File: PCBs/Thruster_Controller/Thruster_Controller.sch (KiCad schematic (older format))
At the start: 30 parts, among them J1 PHASE_A, J2 PHASE_B, J3 PHASE_C, J4 Conn_01x01, J5 Pogo Conn, J6 Conn_01x01, J7 PWRIN, U2 RTQ2569-50GQW, U3 MCP2515, U8 MCP2562, Y1 20MHz

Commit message: Layout
- Trying out different layout approaches
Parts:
- removed J7: PWRIN, MCU_Powertrain:AMASS_XT60-M, symbol Connector_Generic:Conn_01x02
- added J? (x2): Conn_01x01, symbol Connector_Generic:Conn_01x01
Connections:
- net +BATT: now also J?.1 (Pin_1)
- net GND: now also J?.1 (Pin_1)
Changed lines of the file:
@@
 Text Notes 2260 5050 0    79   Italic 16
 3.3V Regulator
-$Comp
-L Connector_Generic:Conn_01x02 J7
-U 1 1 5E5819AC
-P 965 5235
-F 0 "J7" H 965 5010 50  0000 C CNN
-F 1 "PWRIN" H 890 5385 50  0001 C CNN
-F 2 "MCU_Powertrain:AMASS_XT60-M" H 965 5235 50  0001 C CNN
-F 3 "~" H 965 5235 50  0001 C CNN
-F 4 "" H 965 5235 50  0001 C CNN "Digikey"
-	1    965  5235
-	-1   0    0    1
-$EndComp
 Wire Wire Line
 	1365 5085 1365 5135
@@
 $EndComp
 Wire Wire Line
-	1165 5235 1365 5235
-Wire Wire Line
-	1365 5235 1365 5285
+	1165 5260 1365 5260
+Wire Wire Line
+	1365 5260 1365 5310
 $Comp
 L power:GND #PWR?
 U 1 1 5E585248
-P 1365 5285
+P 1365 5310
 AR Path="/5E20A2BB/5E585248" Ref="#PWR?"  Part="1"
 AR Path="/5E585248" Ref="#PWR0111"  Part="1"
-F 0 "#PWR0111" H 1365 5035 50  0001 C CNN
-F 1 "GND" H 1515 5210 50  0000 C CNN
-F 2 "" H 1365 5285 50  0001 C CNN
-F 3 "" H 1365 5285 50  0001 C CNN
-	1    1365 5285
+F 0 "#PWR0111" H 1365 5060 50  0001 C CNN
+F 1 "GND" H 1515 5235 50  0000 C CNN
+F 2 "" H 1365 5310 50  0001 C CNN
+F 3 "" H 1365 5310 50  0001 C CNN
+	1    1365 5310
 	1    0    0    -1
 $EndComp
@@
 	1    0    0    -1
 $EndComp
+$Comp
+L Connector_Generic:Conn_01x01 J?
+U 1 1 5EED2A54
+P 965 5135
+F 0 "J?" H 1130 5140 50  0000 C CNN
+F 1 "Conn_01x01" H 883 5001 50  0001 C CNN
+F 2 "" H 965 5135 50  0001 C CNN
+F 3 "~" H 965 5135 50  0001 C CNN
+	1    965  5135
+	-1   0    0    1
+$EndComp
+$Comp
+L Connector_Generic:Conn_01x01 J?
+U 1 1 5EED568B
+P 965 5260
+F 0 "J?" H 1135 5265 50  0000 C CNN
+F 1 "Conn_01x01" H 883 5126 50  0001 C CNN
+F 2 "" H 965 5260 50  0001 C CNN
+F 3 "~" H 965 5260 50  0001 C CNN
+	1    965  5260
+	-1   0    0    1
+$EndComp
 $EndSCHEMATC

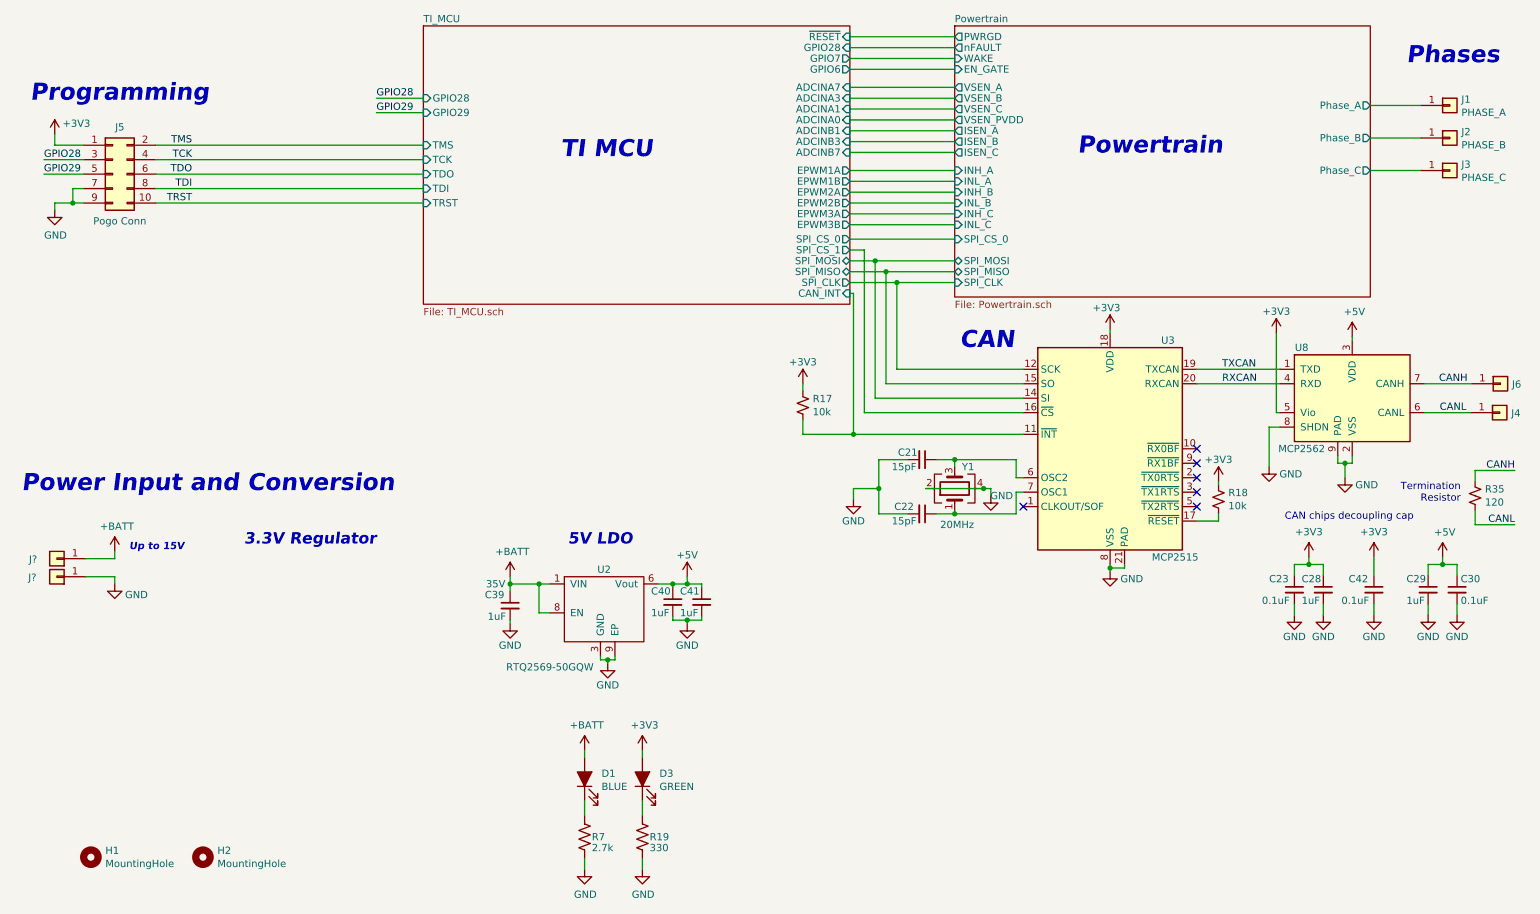
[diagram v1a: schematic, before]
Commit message: 3V3 Regulator
- Added in new 3V3 switching regulator, should save $$$ from the old one and about 1W versus a standard LDO
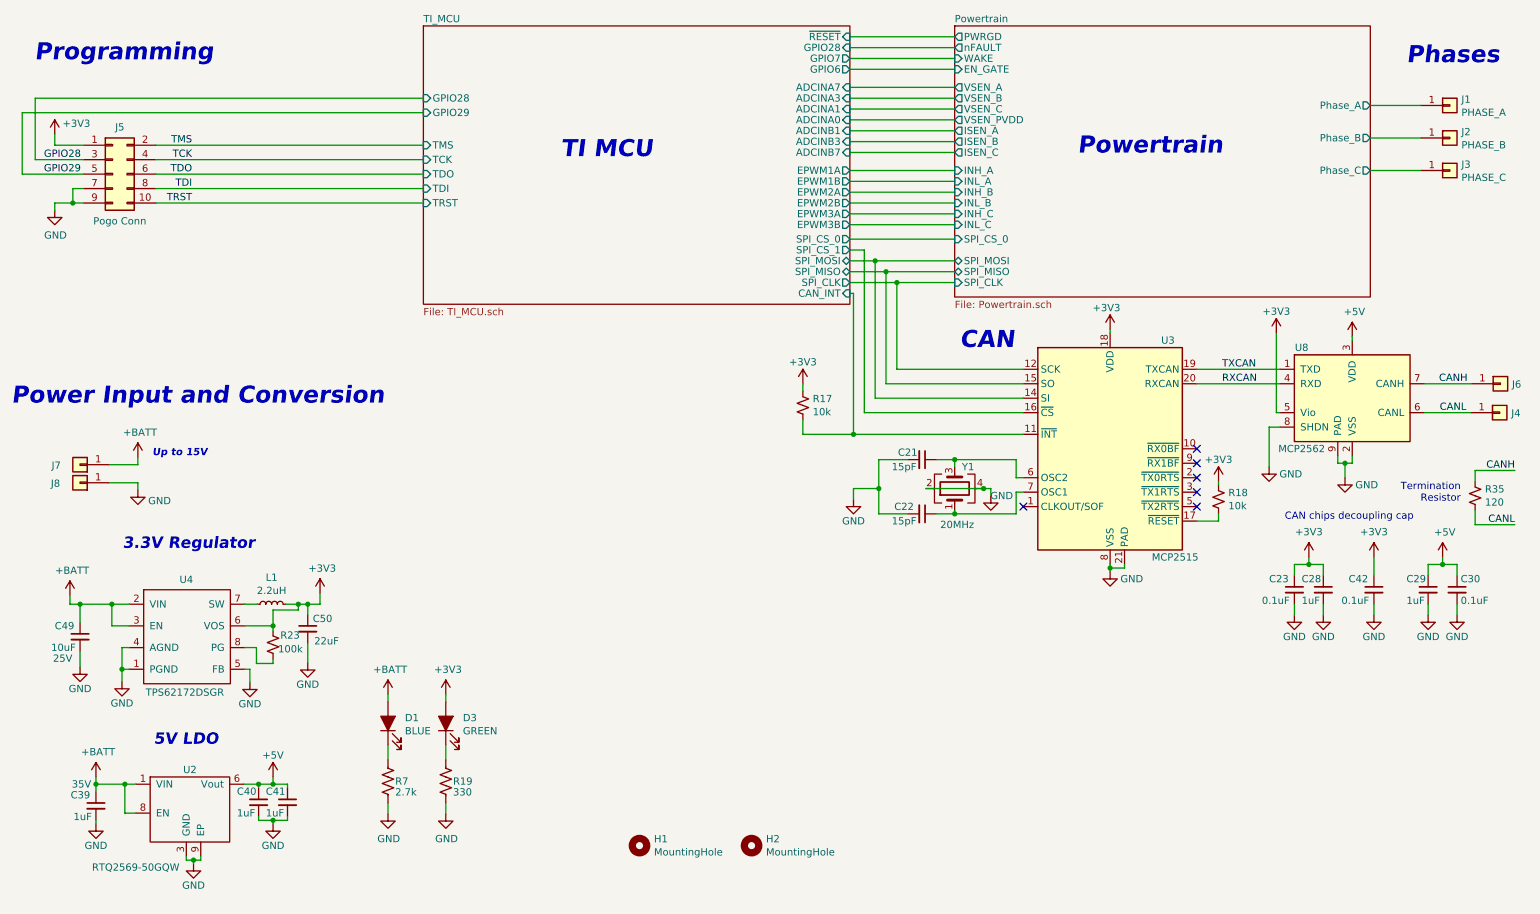
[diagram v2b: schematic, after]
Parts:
- added C49: 10uF, Capacitors_SMD:C_0805, symbol Device:C_Small
- added C50: 22uF, Capacitors_SMD:C_0603, symbol Device:C_Small
- added L1: 2.2uH, Inductors_SMD:L_0805, symbol Device:L_Small
- added R23: 100k, Resistors_SMD:R_0402_NoSilk, symbol Device:R_Small_US
- added U4: TPS62172DSGR, Thruster_Controller:8-Pin_WSON, symbol Thruster_Controller:TPS62172DSGR
- gave numbers to parts that had none: 2
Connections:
- net +3V3: now also C50.1, L1.2, R23.1, U4.6 (VOS)
- net +BATT: now also C49.1, U4.2 (VIN), U4.3 (EN)
- net GND: now also C49.2, C50.2, U4.1 (PGND), U4.4 (AGND), U4.5 (FB)
- new net: L1.1, U4.7 (SW)
- new net: R23.2, U4.8 (PG)
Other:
- moved on the sheet: C39, C40, C41, D1, D3, H1, H2, J7, J8, R19, R7, U2

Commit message: More Layout and Routing
- Powertrain is mostly done, very tight and the phase and bus pads are sized and placed!
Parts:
- J1, J2, J3: footprint MCU_Powertrain:3mm_Bullet_RA -> Thruster_Controller:Phase_Pad
- J7, J8: footprint (none) -> Thruster_Controller:Bus_Pad
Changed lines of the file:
@@
 F 0 "J1" H 10680 2042 50  0000 L CNN
 F 1 "PHASE_A" H 10680 1951 50  0000 L CNN
-F 2 "MCU_Powertrain:3mm_Bullet_RA" H 10600 2000 50  0001 C CNN
+F 2 "Thruster_Controller:Phase_Pad" H 10600 2000 50  0001 C CNN
 F 3 "~" H 10600 2000 50  0001 C CNN
 	1    10600 2000
@@
 F 0 "J2" H 10680 2267 50  0000 L CNN
 F 1 "PHASE_B" H 10680 2176 50  0000 L CNN
-F 2 "MCU_Powertrain:3mm_Bullet_RA" H 10600 2225 50  0001 C CNN
+F 2 "Thruster_Controller:Phase_Pad" H 10600 2225 50  0001 C CNN
 F 3 "~" H 10600 2225 50  0001 C CNN
 	1    10600 2225
@@
 F 0 "J3" H 10680 2492 50  0000 L CNN
 F 1 "PHASE_C" H 10680 2401 50  0000 L CNN
-F 2 "MCU_Powertrain:3mm_Bullet_RA" H 10600 2450 50  0001 C CNN
+F 2 "Thruster_Controller:Phase_Pad" H 10600 2450 50  0001 C CNN
 F 3 "~" H 10600 2450 50  0001 C CNN
 	1    10600 2450
@@
 F 0 "J7" H 1290 4490 50  0000 C CNN
 F 1 "Conn_01x01" H 1043 4351 50  0001 C CNN
-F 2 "" H 1125 4485 50  0001 C CNN
+F 2 "Thruster_Controller:Bus_Pad" H 1125 4485 50  0001 C CNN
 F 3 "~" H 1125 4485 50  0001 C CNN
 	1    1125 4485
@@
 F 0 "J8" H 1295 4615 50  0000 C CNN
 F 1 "Conn_01x01" H 1043 4476 50  0001 C CNN
-F 2 "" H 1125 4610 50  0001 C CNN
+F 2 "Thruster_Controller:Bus_Pad" H 1125 4610 50  0001 C CNN
 F 3 "~" H 1125 4610 50  0001 C CNN
 	1    1125 4610

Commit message: More Layout + Routing
- Added 3V3 converter
- Moved DRV passives to directly underneath DRV chip on top layer
- Fit power indication LEDs!
- Think there should be enough space for everything! Routing to the left of TI chip and CAN controller to the right
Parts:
- H1, H2: footprint Mounting_Holes:MountingHole_2.2mm_M2 -> Thruster_Controller:MountingHole_M2
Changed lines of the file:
@@
 F 0 "H2" H 5870 7166 50  0000 L CNN
 F 1 "MountingHole" H 5870 7075 50  0000 L CNN
-F 2 "Mounting_Holes:MountingHole_2.2mm_M2" H 5770 7120 50  0001 C CNN
+F 2 "Thruster_Controller:MountingHole_M2" H 5770 7120 50  0001 C CNN
 F 3 "~" H 5770 7120 50  0001 C CNN
 	1    5770 7120
@@
 F 0 "H1" H 5095 7166 50  0000 L CNN
 F 1 "MountingHole" H 5095 7075 50  0000 L CNN
-F 2 "Mounting_Holes:MountingHole_2.2mm_M2" H 4995 7120 50  0001 C CNN
+F 2 "Thruster_Controller:MountingHole_M2" H 4995 7120 50  0001 C CNN
 F 3 "~" H 4995 7120 50  0001 C CNN
 	1    4995 7120

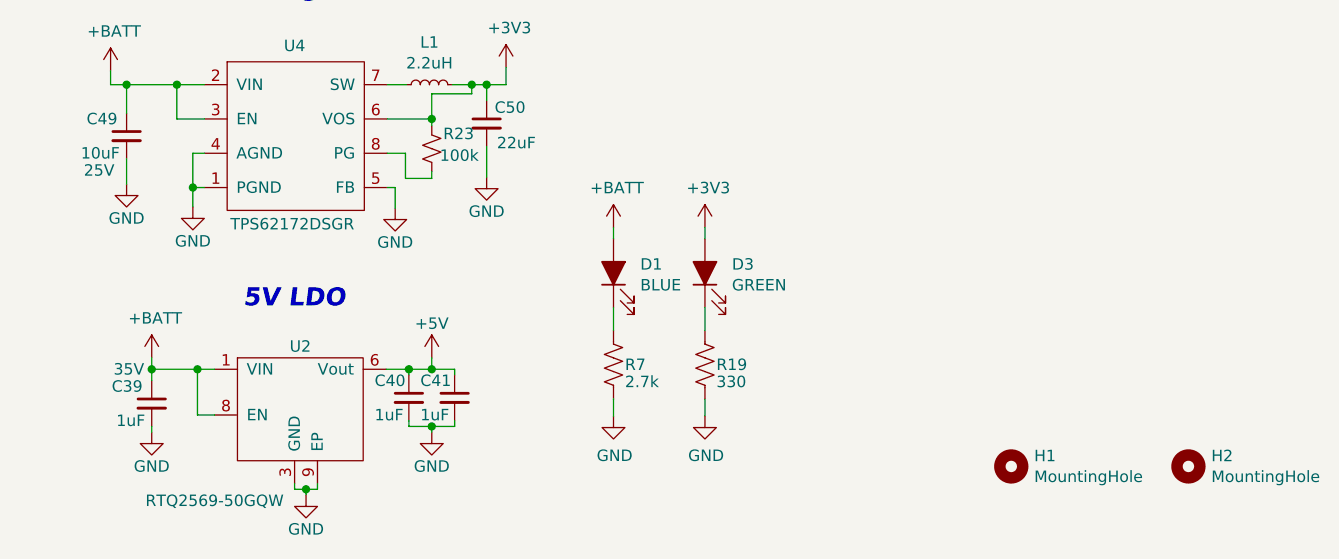
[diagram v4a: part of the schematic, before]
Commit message: Initial Routing Finished
- All layout and routing initially finished
- Still need to clean up silkscreen and any routing blemishes
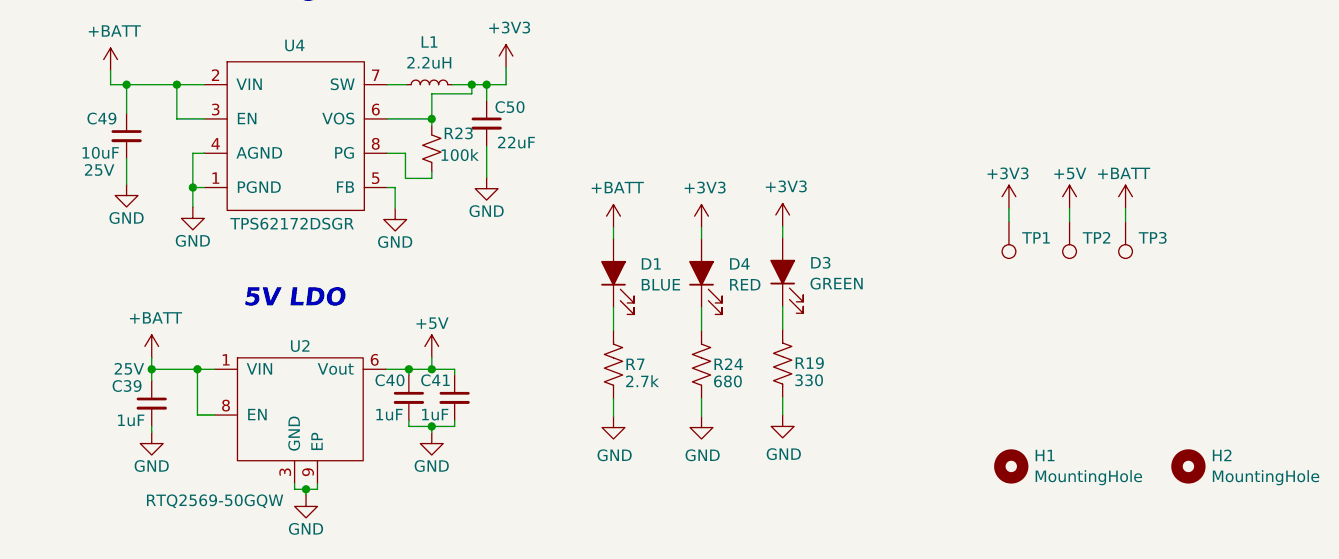
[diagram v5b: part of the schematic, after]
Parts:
- added D4: RED, LEDs:LED_0603, symbol Device:LED_ALT
- added R24: 680, Resistors_SMD:R_0603, symbol Device:R_US
- added TP1, TP2, TP3: TestPoint, Thruster_Controller:TestPoint_Pad_D1.0mm, symbol Connector:TestPoint
- C21: footprint Capacitors_SMD:C_0603 -> Capacitors_SMD:C_0402
- C22: footprint Capacitors_SMD:C_0603 -> Capacitors_SMD:C_0402; Digikey 311-1060-1-ND -> 732-7456-1-ND
- C23, C30, C42: footprint Capacitors_SMD:C_0603 -> Capacitors_SMD:C_0402; Digikey 1276-CL10B104KB8NNNLCT-ND -> 490-10698-1-ND
- C28, C29, C40, C41: footprint Capacitors_SMD:C_0805 -> Capacitors_SMD:C_0603; Digikey 399-8011-1-ND -> 1276-1102-1-ND
- C39: footprint Capacitors_SMD:C_0805 -> Capacitors_SMD:C_0603; Digikey 311-1909-1-ND -> 1276-1102-1-ND; Voltage 35V -> 25V
- D1: Digikey 160-1827-1-ND -> 732-4966-1-ND
- D3: Digikey 160-1446-1-ND -> 732-4980-1-ND
- J4, J6: footprint (none) -> Thruster_Controller:CAN_Pad
- R17, R18: footprint Resistors_SMD:R_0805 -> Resistors_SMD:R_0402; Digikey 311-10.0KCRCT-ND -> 311-10KJRCT-ND
- R35: footprint Resistors_SMD:R_0805 -> Resistors_SMD:R_0402; Digikey A129738CT-ND -> 311-120JRCT-ND
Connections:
- net +3V3: now also D4.2 (A), TP1.1
- net +5V: now also TP2.1
- net +BATT: now also TP3.1
- net GND: now also R24.2
- new net: D4.1 (K), R24.1
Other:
- moved on the sheet: D3, R19

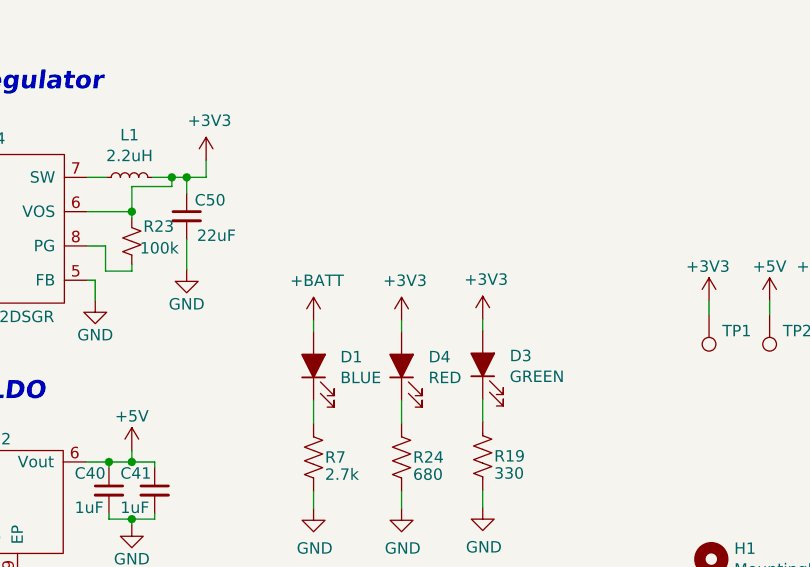
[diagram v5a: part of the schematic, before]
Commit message: Silk and Routing
- Fixed 5V LED indicator
- Small layout and routing cleanups
- Cleaned up Silkscreen
- Board is "finished" !!
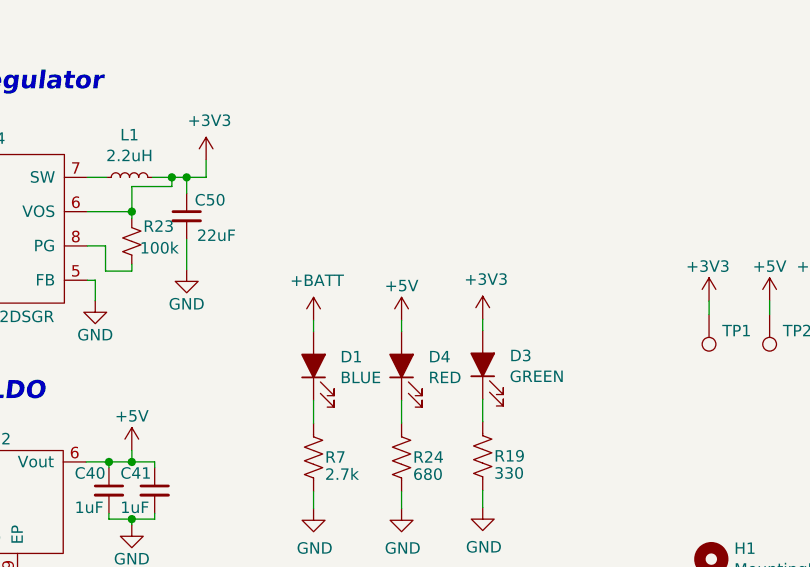
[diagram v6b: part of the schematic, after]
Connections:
- net +3V3: no longer D4.2 (A)
- net +5V: now also D4.2 (A)
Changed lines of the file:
@@
 	3995 6120 3995 6070
-$Comp
-L power:+3V3 #PWR?
-U 1 1 5E5672BA
-P 3995 6070
-AR Path="/5E20A2BB/5E5672BA" Ref="#PWR?"  Part="1"
-AR Path="/5E5672BA" Ref="#PWR0108"  Part="1"
-F 0 "#PWR0108" H 3995 5920 50  0001 C CNN
-F 1 "+3V3" H 4010 6243 50  0000 C CNN
-F 2 "" H 3995 6070 50  0001 C CNN
-F 3 "" H 3995 6070 50  0001 C CNN
-	1    3995 6070
-	1    0    0    -1
-$EndComp
 $Comp
 L Device:LED_ALT D?
@@
 Wire Wire Line
 	3640 6425 3640 6525
-Wire Wire Line
-	3640 6125 3640 6075
-$Comp
-L power:+3V3 #PWR?
-U 1 1 5E9CA972
-P 3640 6075
-AR Path="/5E20A2BB/5E9CA972" Ref="#PWR?"  Part="1"
-AR Path="/5E9CA972" Ref="#PWR0154"  Part="1"
-F 0 "#PWR0154" H 3640 5925 50  0001 C CNN
-F 1 "+3V3" H 3655 6248 50  0000 C CNN
-F 2 "" H 3640 6075 50  0001 C CNN
-F 3 "" H 3640 6075 50  0001 C CNN
-	1    3640 6075
-	1    0    0    -1
-$EndComp
 $Comp
 L Device:LED_ALT D?
@@
 	0    -1   -1   0
 $EndComp
+$Comp
+L power:+3V3 #PWR?
+U 1 1 5E5672BA
+P 3995 6070
+AR Path="/5E20A2BB/5E5672BA" Ref="#PWR?"  Part="1"
+AR Path="/5E5672BA" Ref="#PWR0108"  Part="1"
+F 0 "#PWR0108" H 3995 5920 50  0001 C CNN
+F 1 "+3V3" H 4010 6243 50  0000 C CNN
+F 2 "" H 3995 6070 50  0001 C CNN
+F 3 "" H 3995 6070 50  0001 C CNN
+	1    3995 6070
+	1    0    0    -1
+$EndComp
+Wire Wire Line
+	3640 6125 3640 6075
+$Comp
+L power:+5V #PWR?
+U 1 1 5EBB5551
+P 3640 6075
+F 0 "#PWR?" H 3640 5925 50  0001 C CNN
+F 1 "+5V" H 3640 6225 50  0000 C CNN
+F 2 "" H 3640 6075 50  0001 C CNN
+F 3 "" H 3640 6075 50  0001 C CNN
+	1    3640 6075
+	1    0    0    -1
+$EndComp
 $EndSCHEMATC
